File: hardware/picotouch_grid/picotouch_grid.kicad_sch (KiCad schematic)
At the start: 125 parts, among them U1 Pico, U2 TS20, U3 TS20

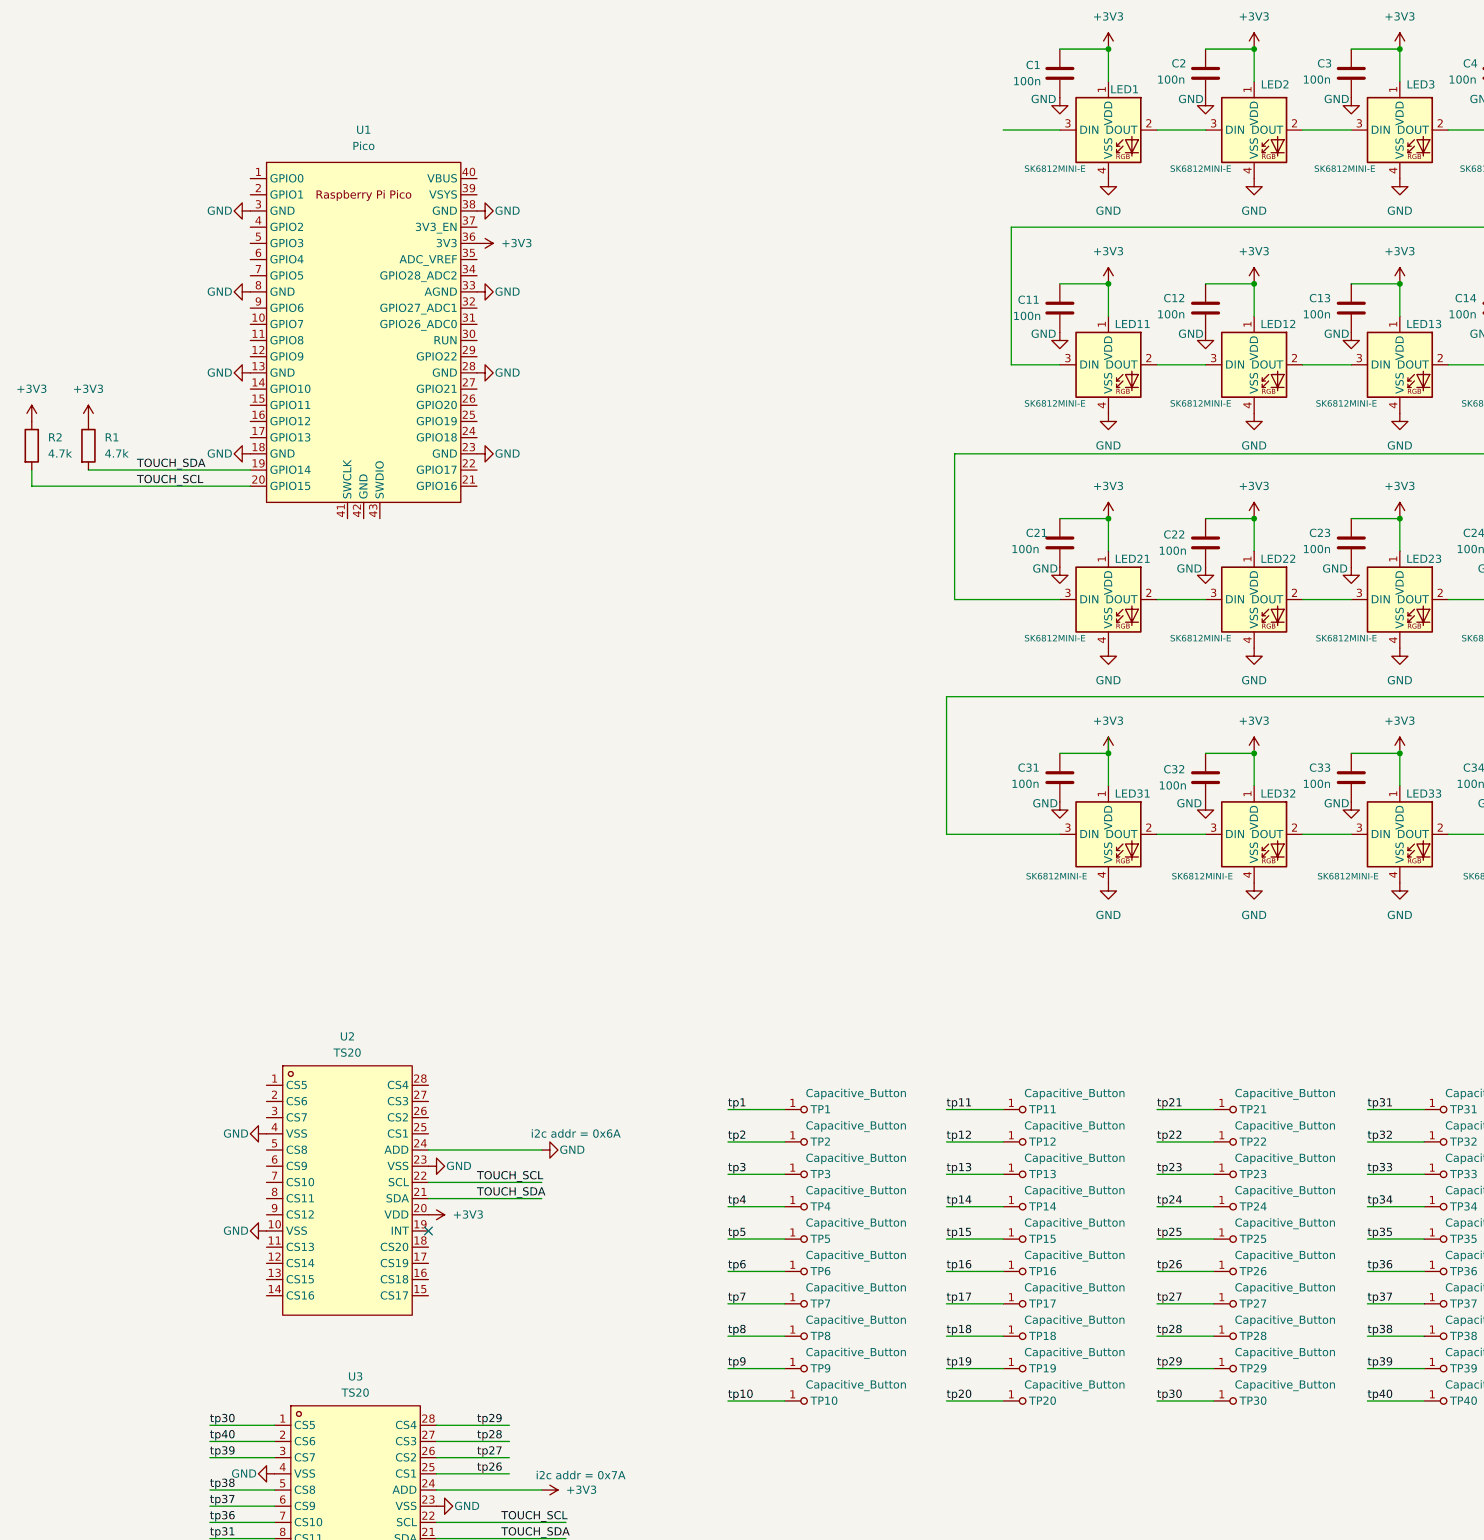
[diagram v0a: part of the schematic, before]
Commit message: more pcb routing done
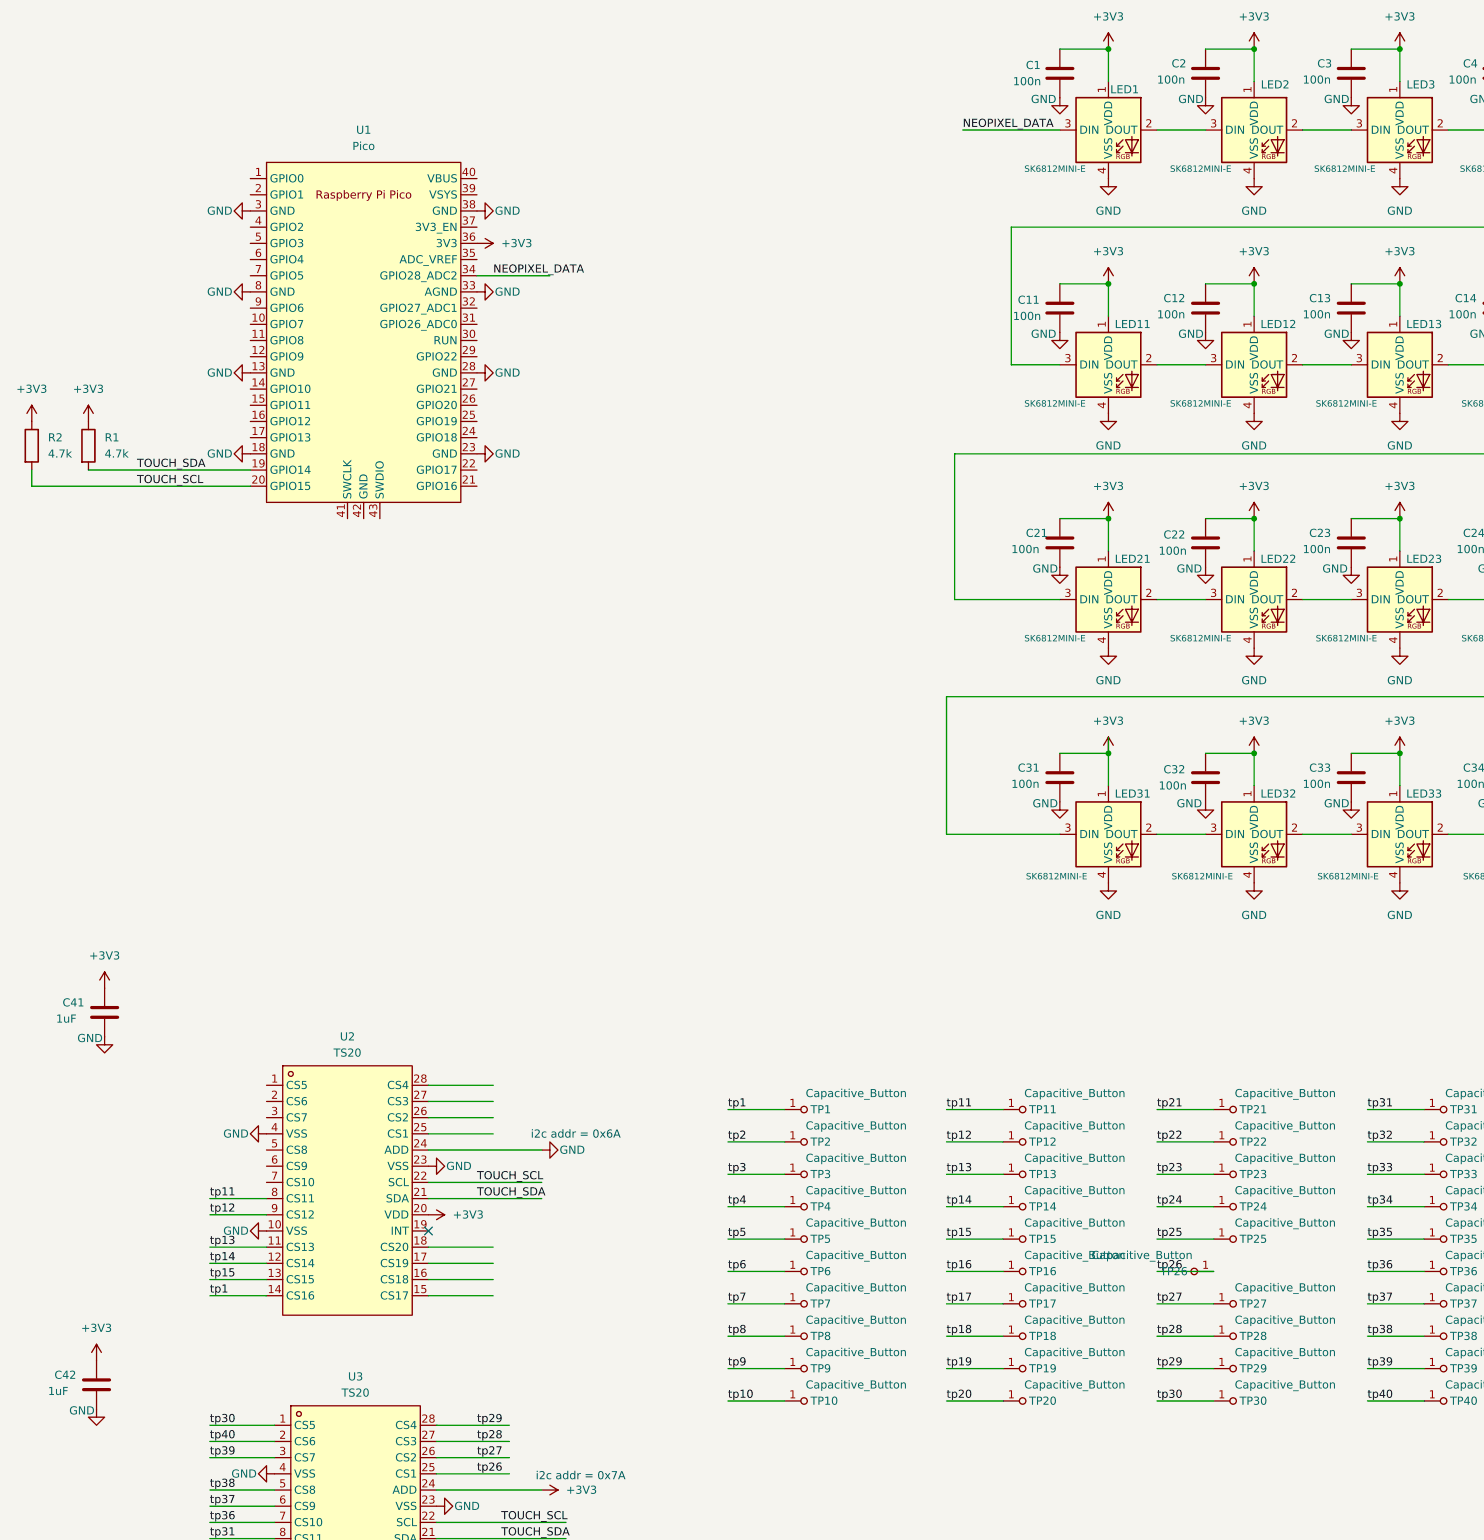
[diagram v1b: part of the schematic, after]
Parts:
- added C41, C42: 1uF, Capacitor_SMD:C_0603_1608Metric, symbol Device:C
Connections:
- net +3V3: now also C41.1, C42.1
- net GND: now also C41.2, C42.2
- net tp1: now also U2.14 (CS16)
- net tp11: now also U2.8 (CS11)
- net tp12: now also U2.9 (CS12)
- net tp13: now also U2.11 (CS13)
- net tp14: now also U2.12 (CS14)
- net tp15: now also U2.13 (CS15)
- net NEOPIXEL_DATA: now reaches LED1.3 (DIN)
- net NEOPIXEL_DATA: now also U1.34 (GPIO28_ADC2)
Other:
- moved on the sheet: TP26

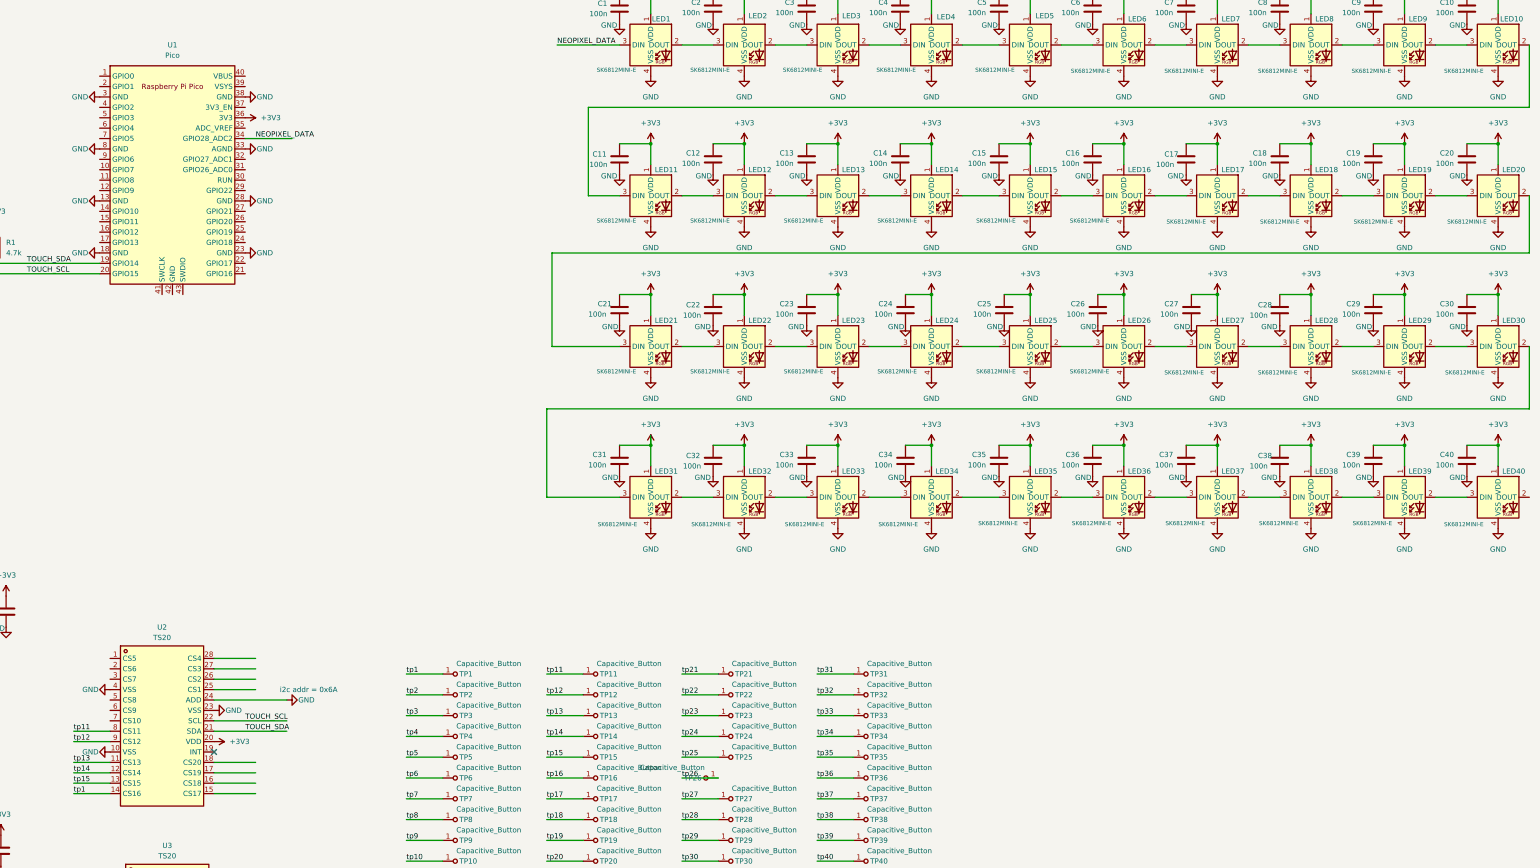
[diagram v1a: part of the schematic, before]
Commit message: pads mostly routed
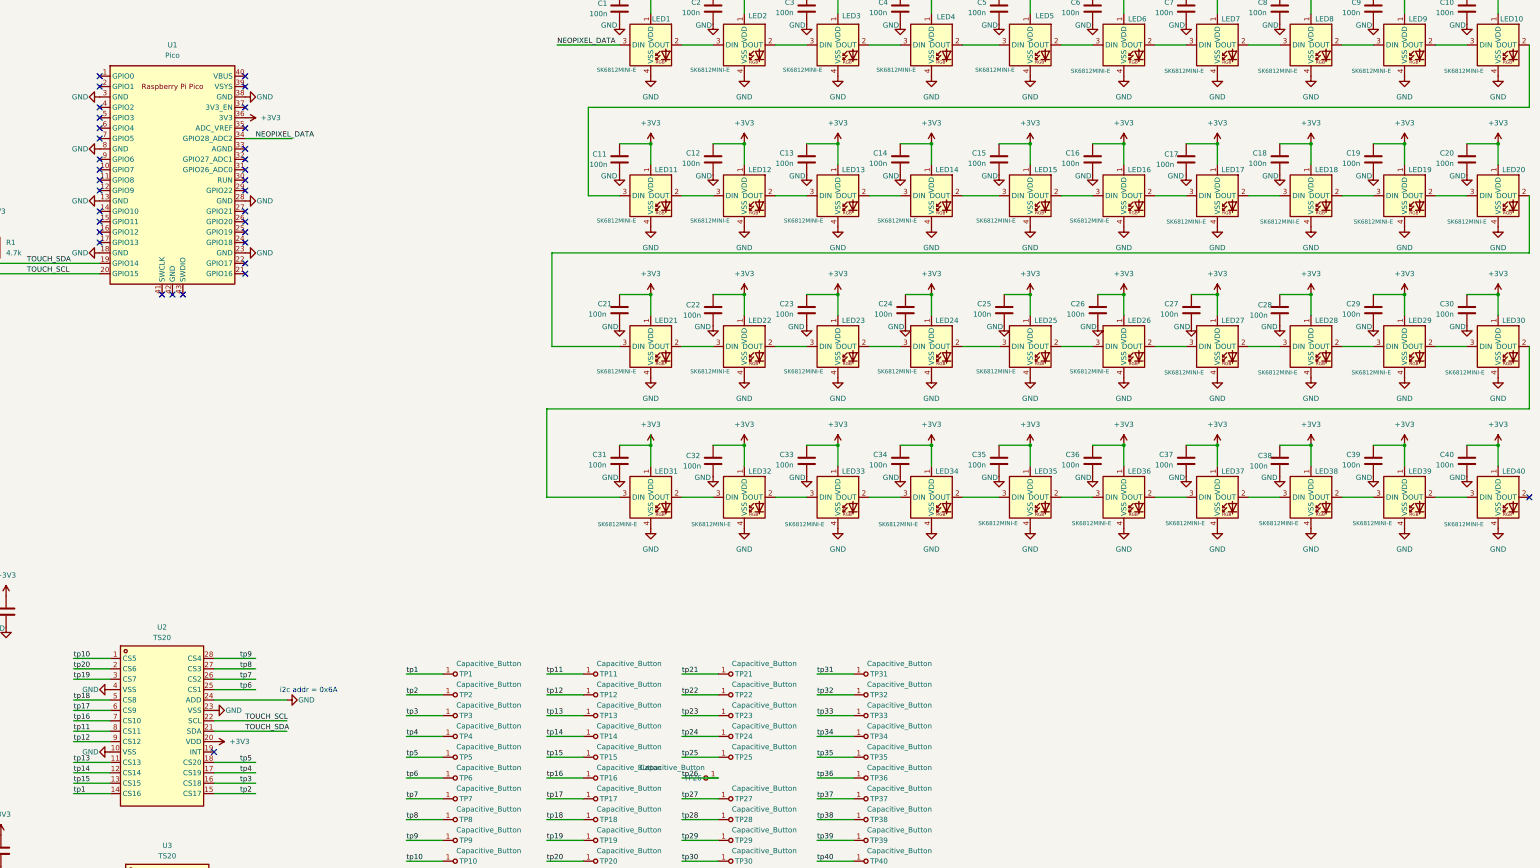
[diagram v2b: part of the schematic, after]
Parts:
- U2, U3: symbol easyeda2kicad:TS20 -> todbot_stuff:TS20_easyeda
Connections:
- net GND: no longer U1.33 (AGND)
- net tp10: now also U2.1 (CS5)
- net tp16: now also U2.7 (CS10)
- net tp17: now also U2.6 (CS9)
- net tp18: now also U2.5 (CS8)
- net tp19: now also U2.3 (CS7)
- net tp2: now also U2.15 (CS17)
- net tp20: now also U2.2 (CS6)
- net tp3: now also U2.16 (CS18)
- net tp4: now also U2.17 (CS19)
- net tp5: now also U2.18 (CS20)
- net tp6: now also U2.25 (CS1)
- net tp7: now also U2.26 (CS2)
- net tp8: now also U2.27 (CS3)
- net tp9: now also U2.28 (CS4)
- no-connect marks 2 -> 35
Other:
- moved on the sheet: C34

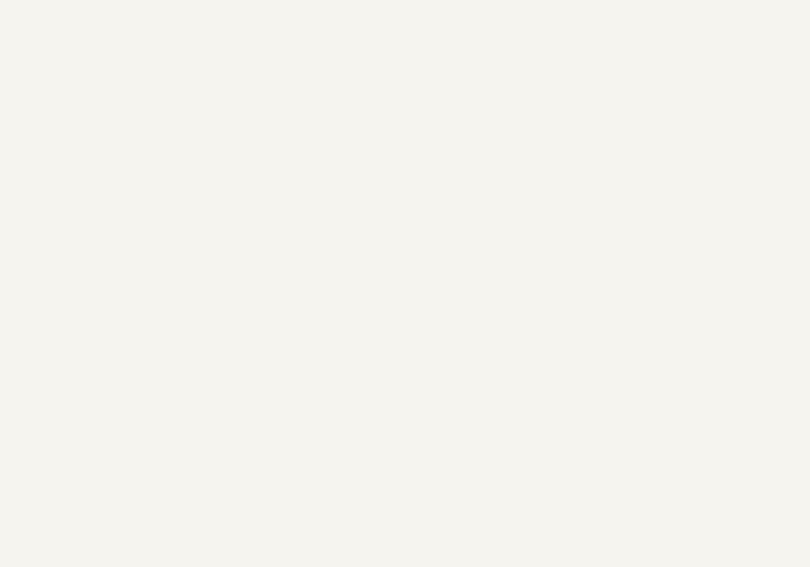
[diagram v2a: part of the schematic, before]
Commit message: added jlcpcb dru rules from "KiCad-DesignRules"
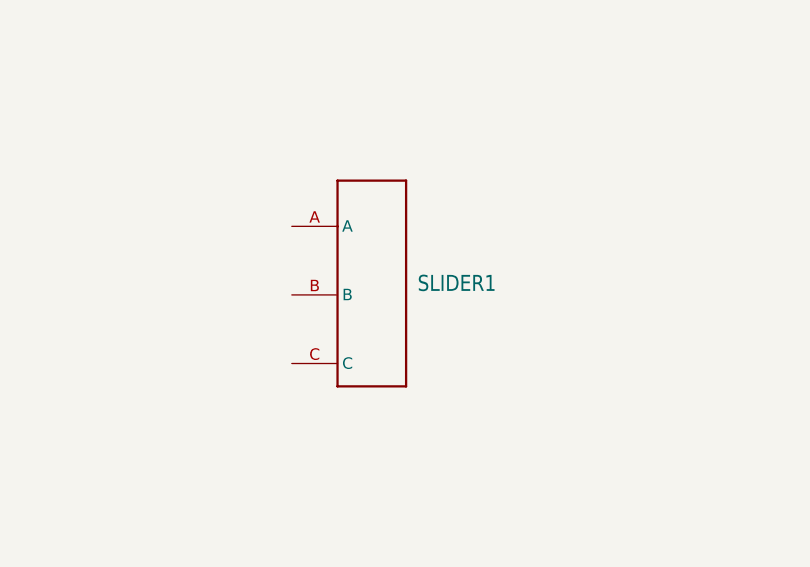
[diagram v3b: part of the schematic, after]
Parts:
- added SLIDER1: ~, todbot_eagle2023:TOUCHSLIDER3_8x40B, symbol todbot_eagle2023:TouchSlider3
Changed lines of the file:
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@@
+		)
+	)
+	(symbol
+		(lib_id "todbot_eagle2023:TouchSlider3")
+		(at 91.44 127 0)
+		(unit 1)
+		(exclude_from_sim no)
+		(in_bom yes)
+		(on_board yes)
+		(dnp no)
+		(fields_autoplaced yes)
+		(property "Reference" "SLIDER1"
+			(at 95.25 125.73 0)
+			(effects
+				(font
+					(size 1.778 1.5113)
+				)
+				(justify left)
+			)
+		)
+		(property "Value" "~"
+			(at 86.36 139.7 0)
+			(effects
+				(font
+					(size 1.778 1.5113)
+				)
+				(justify left bottom)
+				(hide yes)
+			)
+		)
+		(property "Footprint" "todbot_eagle2023:TOUCHSLIDER3_8x40B"
+			(at 91.44 127 0)
+			(effects
+				(font
+					(size 1.27 1.27)
+				)
+				(hide yes)
+			)
+		)
+		(property "Datasheet" ""
+			(at 91.44 127 0)
+			(effects
+				(font
+					(size 1.27 1.27)
+				)
+				(hide yes)
+			)
+		)
+		(property "Description" ""
+			(at 91.44 127 0)
+			(effects
+				(font
+					(size 1.27 1.27)
+				)
+				(hide yes)
+			)
+		)
+		(pin "C"
+		)
+		(pin "B"
+		)
+		(pin "A"
+		)
+		(instances
+			(project "picotouch_grid"
+				(path "/036e8f10-ba17-4cdc-95e8-e722ded3fffe"
+					(reference "SLIDER1")
+					(unit 1)
+				)
+			)
 		)
 	)

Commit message: pcb: added midi in/out, pwm audio out
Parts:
- removed SLIDER1: ~, todbot_eagle2023:TOUCHSLIDER3_8x40B, symbol todbot_eagle2023:TouchSlider3
- added C43, C44: 100n, Capacitor_SMD:C_0603_1608Metric, symbol Device:C
- added C45: 47uF, Capacitor_SMD:C_0603_1608Metric, symbol Device:C
- added D1: 1N4148, Diode_SMD:D_SOD-123, symbol Device:D
- added DISP1: HS96L03W2C03, todbot_stuff:OLED-TH_under_L27.8-W27.2-P2.54_C9900033791, symbol easyeda2kicad:HS96L03W2C03
- added J1, J2, J3: TRRS, Keebio-Parts:TRRS-PJ-320D, symbol keebio:TRRS
- added R10: 1.8k, Resistor_SMD:R_0603_1608Metric, symbol Device:R
- added R3, R4: 4.7k, Resistor_SMD:R_0603_1608Metric, symbol Device:R
- added R5, R8: 200, Resistor_SMD:R_0603_1608Metric, symbol Device:R
- added R6: 33, Resistor_SMD:R_0603_1608Metric, symbol Device:R
- added R7: 10, Resistor_SMD:R_0603_1608Metric, symbol Device:R
- added R9: 100, Resistor_SMD:R_0603_1608Metric, symbol Device:R
- added U5: H11L1, Package_DIP:DIP-6_W8.89mm_SMDSocket_LongPads, symbol Isolator:H11L1
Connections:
- net +3V3: now also C43.1, DISP1.2 (VCC), R3.1, R4.1, R6.2, U5.6
- net GND: now also C43.2, C44.2, DISP1.1 (GND), J1.1 (SLEEVE), J2.1 (SLEEVE), J3.1 (SLEEVE), R10.2, R9.2, U5.5
- net TOUCH_SCL: now also U1.22 (GPIO17), R3.2; no longer R2.2, U1.20 (GPIO15)
- net TOUCH_SDA: now also U1.21 (GPIO16), R4.2; no longer R1.2, U1.19 (GPIO14)
- net MIDI_OUT: now reaches U1.11 (GPIO8)
- net MIDI_OUT: now also R7.1
- net MIDI_IN: now reaches U1.12 (GPIO9)
- net MIDI_IN: now also U5.4
- net PWM_AUDIO: now reaches U1.17 (GPIO13)
- net PWM_AUDIO: now also R8.1
- new net: D1.1 (K), R5.2, U5.1
- new net: D1.2 (A), J1.2 (TIP), U5.2
- new net: J2.3 (RING1), R6.1
- new net: C44.1, C45.2, R8.2, R9.1
- new net: J2.2 (TIP), R7.2
- new net: J1.3 (RING1), R5.1
- new net AUDIO_OUT: C45.1, J3.2 (TIP), J3.3 (RING1), R10.1
- new net DISP_SCL: DISP1.3 (SCL), R2.2, U1.20 (GPIO15)
- new net DISP_SDA: DISP1.4 (SDA), R1.2, U1.19 (GPIO14)
- no-connect marks 35 -> 30
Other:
- moved on the sheet: C41, C42, TP1, TP10, TP11, TP12, TP13, TP14, TP15, TP16, TP17, TP18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

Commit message: pcb: add more buttons, clean up layout of sch & pcb
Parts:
- added H1, H2, H3, H4: MountingHole, MountingHole:MountingHole_2.7mm_M2.5, symbol Mechanical:MountingHole
- added R11, R12, R13, R14, R15, R16, R17: 1M, Resistor_SMD:R_0603_1608Metric, symbol Device:R
- added SLIDER1: ~, todbot_eagle2023:TOUCHSLIDER3_8x40B, symbol todbot_eagle2023:TouchSlider-3sectors
- added TP41, TP42, TP43, TP44: Capacitive Button, SparkFun-Switch:Pad-CapacitiveTouch, symbol SparkFun-Switch:Capacitive Button
- added rx1: rx, TestPoint:TestPoint_Pad_D2.0mm, symbol Connector:TestPoint
- added tx1: tx, TestPoint:TestPoint_Pad_D2.0mm, symbol Connector:TestPoint
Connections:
- net GND: now also R11.1, R12.1, R13.1, R14.1, R15.1, R16.1, R17.1
- net UART_TX: now reaches U1.1 (GPIO0)
- net UART_TX: now also tx1.1
- net UART_RX: now reaches U1.2 (GPIO1)
- net UART_RX: now also rx1.1
- net FADER1A: now reaches U1.4 (GPIO2)
- net FADER1A: now also R11.2, SLIDER1.A
- net FADER1B: now reaches U1.5 (GPIO3)
- net FADER1B: now also R12.2, SLIDER1.B
- net FADER1C: now reaches U1.6 (GPIO4)
- net FADER1C: now also R13.2, SLIDER1.C
- new net: R16.2, TP43.1 (A)
- new net: R17.2, TP44.1 (A)
- new net: R14.2, TP41.1 (A)
- new net: R15.2, TP42.1 (A)
- no-connect marks 30 -> 25

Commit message: pcb: tune button layout
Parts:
- added H5, H6: MountingHole, MountingHole:MountingHole_2.1mm, symbol Mechanical:MountingHole
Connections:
- net BUT3: now reaches R16.2, TP43.1 (A)
- net BUT3: now also U1.26 (GPIO20)
- net BUT4: now reaches R17.2, TP44.1 (A)
- net BUT4: now also U1.27 (GPIO21)
- net BUT1: now reaches R14.2, TP41.1 (A)
- net BUT1: now also U1.24 (GPIO18)
- net BUT2: now reaches U1.25 (GPIO19)
- net BUT2: now also R15.2, TP42.1 (A)
- no-connect marks 25 -> 21
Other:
- moved on the sheet: H1, H2, H3, H4
